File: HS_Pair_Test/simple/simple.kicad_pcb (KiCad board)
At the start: 2 copper layers, 43 x 11 mm, 3 parts, among them P101 CONN_01X02, P102 CONN_01X02, P103 CONN_01X02

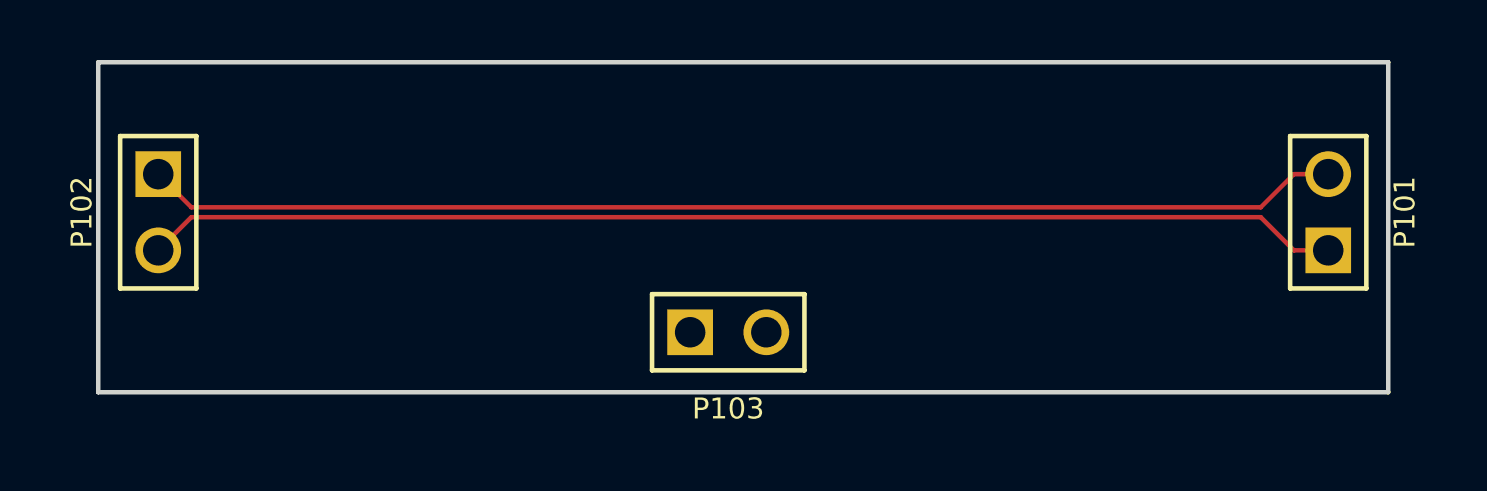
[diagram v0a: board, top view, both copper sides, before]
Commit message: changed the simple example with a SMT connector
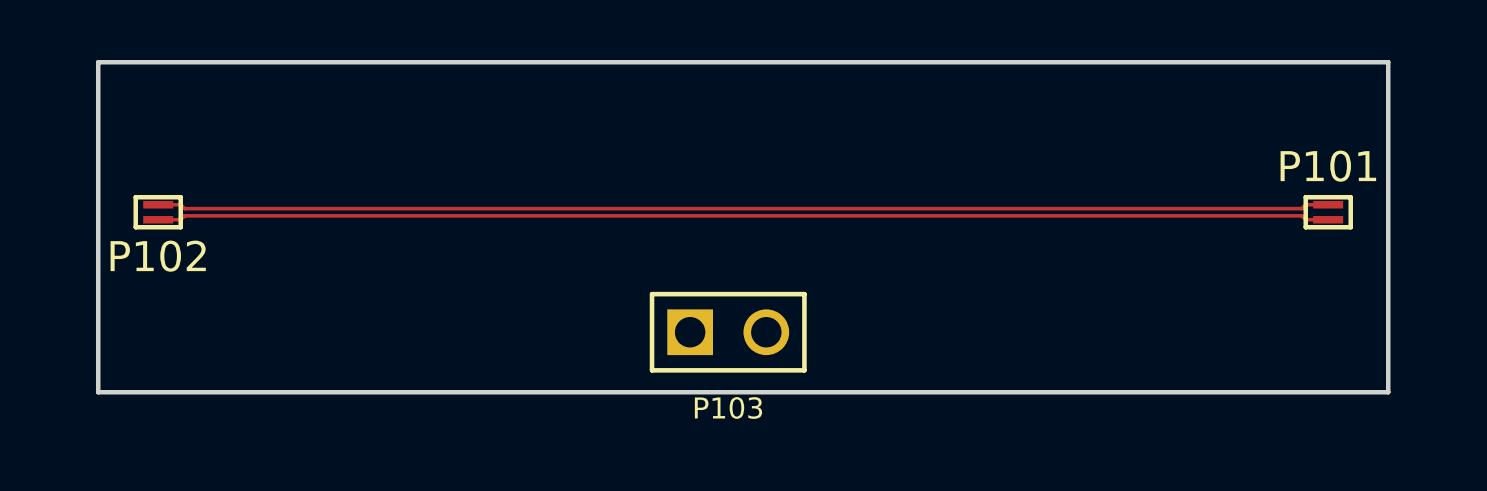
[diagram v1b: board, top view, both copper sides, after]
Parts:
- P101, P102: footprint Connectors_254mm:pin_array_2x1 -> test:TEST_01x02_05mm
- turned P101 to 180 degrees
- turned P102 to 0 degrees
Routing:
- net /HS_P: track 39.9 -> 39.1 mm
- net /HS_N: track 39.9 -> 39.1 mm
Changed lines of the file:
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@@
-(kicad_pcb (version 4) (host pcbnew "(2015-08-16 BZR 6097, Git b384c94)-product")
+(kicad_pcb (version 4) (host pcbnew "(2015-08-01 BZR 6032, Git 6a6a55f)-product")
   (general
     (links 3)
     (no_connects 2)
-    (area 125.924999 99.924999 169.075001 111.075001)
+    (area 122.891667 99.924999 172.108334 112.316)
     (thickness 1.6)
     (drawings 4)
-    (tracks 8)
+    (tracks 10)
     (zones 0)
     (modules 3)
@@
     (pad_to_mask_clearance 0.2)
     (aux_axis_origin 0 0)
-    (visible_elements FFFFFF7F)
+    (visible_elements 7FFFFFFF)
     (pcbplotparams
       (layerselection 0x00000_80000001)
-      (usegerberextensions false)
+      (usegerberextensions true)
       (excludeedgelayer true)
       (linewidth 0.100000)
@@
   )
   (module Connectors_254mm:pin_array_2x1 (layer F.Cu)
-    (at 167 105 90)
-    (descr "Connecteurs 2 pins")
-    (tags "CONN DEV")
-    (fp_text reference P101 (at 0 2.55 90) (layer F.SilkS)
-      (effects (font (size 0.7 0.7) (thickness 0.152)))
-    )
-    (fp_text value CONN_01X02 (at 0 -1.905 90) (layer F.SilkS) hide
-      (effects (font (size 0.762 0.762) (thickness 0.1524)))
-    )
-    (fp_line (start -2.54 1.27) (end -2.54 -1.27) (layer F.SilkS) (width 0.1524))
-    (fp_line (start -2.54 -1.27) (end 2.54 -1.27) (layer F.SilkS) (width 0.1524))
-    (fp_line (start 2.54 -1.27) (end 2.54 1.27) (layer F.SilkS) (width 0.1524))
-    (fp_line (start 2.54 1.27) (end -2.54 1.27) (layer F.SilkS) (width 0.1524))
-    (pad 1 thru_hole rect (at -1.27 0 90) (size 1.524 1.524) (drill 1.016) (layers *.Cu *.Mask F.SilkS)
-      (net 2 /HS_P))
-    (pad 2 thru_hole circle (at 1.27 0 90) (size 1.524 1.524) (drill 1.016) (layers *.Cu *.Mask F.SilkS)
-      (net 3 /HS_N))
-    (model pin_array/pins_array_2x1.wrl
-      (at (xyz 0 0 0))
-      (scale (xyz 1 1 1))
-      (rotate (xyz 0 0 0))
-    )
-  )
-  (module Connectors_254mm:pin_array_2x1 (layer F.Cu)
-    (at 128 105 270)
-    (descr "Connecteurs 2 pins")
-    (tags "CONN DEV")
-    (fp_text reference P102 (at 0 2.55 270) (layer F.SilkS)
-      (effects (font (size 0.7 0.7) (thickness 0.152)))
-    )
-    (fp_text value CONN_01X02 (at 0 -1.905 270) (layer F.SilkS) hide
-      (effects (font (size 0.762 0.762) (thickness 0.1524)))
-    )
-    (fp_line (start -2.54 1.27) (end -2.54 -1.27) (layer F.SilkS) (width 0.1524))
-    (fp_line (start -2.54 -1.27) (end 2.54 -1.27) (layer F.SilkS) (width 0.1524))
-    (fp_line (start 2.54 -1.27) (end 2.54 1.27) (layer F.SilkS) (width 0.1524))
-    (fp_line (start 2.54 1.27) (end -2.54 1.27) (layer F.SilkS) (width 0.1524))
-    (pad 1 thru_hole rect (at -1.27 0 270) (size 1.524 1.524) (drill 1.016) (layers *.Cu *.Mask F.SilkS)
-      (net 3 /HS_N))
-    (pad 2 thru_hole circle (at 1.27 0 270) (size 1.524 1.524) (drill 1.016) (layers *.Cu *.Mask F.SilkS)
-      (net 2 /HS_P))
-    (model pin_array/pins_array_2x1.wrl
-      (at (xyz 0 0 0))
-      (scale (xyz 1 1 1))
-      (rotate (xyz 0 0 0))
-    )
-  )
-  (module Connectors_254mm:pin_array_2x1 (layer F.Cu)
     (at 147 109)
     (descr "Connecteurs 2 pins")
@@
     )
   )
+  (module test:TEST_01x02_05mm (layer F.Cu)
+    (at 167 105 180)
+    (attr smd)
+    (fp_text reference P101 (at 0 1.5 180) (layer F.SilkS)
+      (effects (font (size 1 1) (thickness 0.15)))
+    )
+    (fp_text value CONN_01X02 (at 0 -0.5 180) (layer F.Fab) hide
+      (effects (font (size 1 1) (thickness 0.15)))
+    )
+    (fp_line (start -0.75 -0.5) (end 0.75 -0.5) (layer F.SilkS) (width 0.15))
+    (fp_line (start 0.75 -0.5) (end 0.75 0.5) (layer F.SilkS) (width 0.15))
+    (fp_line (start 0.75 0.5) (end -0.75 0.5) (layer F.SilkS) (width 0.15))
+    (fp_line (start -0.75 0.5) (end -0.75 -0.5) (layer F.SilkS) (width 0.15))
+    (pad 1 smd rect (at 0 -0.25 180) (size 1 0.25) (layers F.Cu F.Paste F.Mask)
+      (net 2 /HS_P))
+    (pad 2 smd rect (at 0 0.25 180) (size 1 0.25) (layers F.Cu F.Paste F.Mask)
+      (net 3 /HS_N))
+  )
+  (module test:TEST_01x02_05mm (layer F.Cu)
+    (at 128 105)
+    (attr smd)
+    (fp_text reference P102 (at 0 1.5) (layer F.SilkS)
+      (effects (font (size 1 1) (thickness 0.15)))
+    )
+    (fp_text value CONN_01X02 (at 0 -0.5) (layer F.Fab) hide
+      (effects (font (size 1 1) (thickness 0.15)))
+    )
+    (fp_line (start -0.75 -0.5) (end 0.75 -0.5) (layer F.SilkS) (width 0.15))
+    (fp_line (start 0.75 -0.5) (end 0.75 0.5) (layer F.SilkS) (width 0.15))
+    (fp_line (start 0.75 0.5) (end -0.75 0.5) (layer F.SilkS) (width 0.15))
+    (fp_line (start -0.75 0.5) (end -0.75 -0.5) (layer F.SilkS) (width 0.15))
+    (pad 1 smd rect (at 0 -0.25) (size 1 0.25) (layers F.Cu F.Paste F.Mask)
+      (net 3 /HS_N))
+    (pad 2 smd rect (at 0 0.25) (size 1 0.25) (layers F.Cu F.Paste F.Mask)
+      (net 2 /HS_P))
+  )
   (gr_line (start 126 111) (end 169 111) (layer Edge.Cuts) (width 0.15))
   (gr_line (start 126 111) (end 126 100) (layer Edge.Cuts) (width 0.15))
   (gr_line (start 169 100) (end 169 111) (layer Edge.Cuts) (width 0.15))
   (gr_line (start 126 100) (end 169 100) (layer Edge.Cuts) (width 0.15))
-  (segment (start 165.857 106.27) (end 167 106.27) (width 0.15) (layer F.Cu) (net 2))
-  (segment (start 128 106.27) (end 129.105001 105.164999) (width 0.15) (layer F.Cu) (net 2))
-  (segment (start 129.105001 105.164999) (end 164.752 105.165) (width 0.15) (layer F.Cu) (net 2))
-  (segment (start 164.752 105.165) (end 165.857 106.27) (width 0.15) (layer F.Cu) (net 2))
-  (segment (start 164.752 104.835) (end 165.857 103.73) (width 0.15) (layer F.Cu) (net 3))
-  (segment (start 128 103.73) (end 129.105001 104.835001) (width 0.15) (layer F.Cu) (net 3))
-  (segment (start 129.105001 104.835001) (end 164.752 104.835) (width 0.15) (layer F.Cu) (net 3))
-  (segment (start 165.857 103.73) (end 167 103.73) (width 0.15) (layer F.Cu) (net 3))
+  (segment (start 128 105.25) (end 128.75 105.25) (width 0.12) (layer F.Cu) (net 2))
+  (segment (start 166.12 105.12) (end 166.25 105.25) (width 0.12) (layer F.Cu) (net 2))
+  (segment (start 128.75 105.25) (end 128.88 105.12) (width 0.12) (layer F.Cu) (net 2))
+  (segment (start 128.88 105.12) (end 166.12 105.12) (width 0.12) (layer F.Cu) (net 2))
+  (segment (start 166.25 105.25) (end 167 105.25) (width 0.12) (layer F.Cu) (net 2))
+  (segment (start 166.12 104.88) (end 166.25 104.75) (width 0.12) (layer F.Cu) (net 3))
+  (segment (start 166.25 104.75) (end 167 104.75) (width 0.12) (layer F.Cu) (net 3))
+  (segment (start 128 104.75) (end 128.75 104.75) (width 0.12) (layer F.Cu) (net 3))
+  (segment (start 128.75 104.75) (end 128.88 104.88) (width 0.12) (layer F.Cu) (net 3))
+  (segment (start 128.88 104.88) (end 166.12 104.88) (width 0.12) (layer F.Cu) (net 3))
   (zone (net 1) (net_name GND) (layer B.Cu) (hatch edge 0.508)
     (connect_pads yes (clearance 0.15))
